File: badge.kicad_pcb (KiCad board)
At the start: 2 copper layers, 90 x 55 mm, 171 parts, among them P1 CONN_8, P2 CONN_11

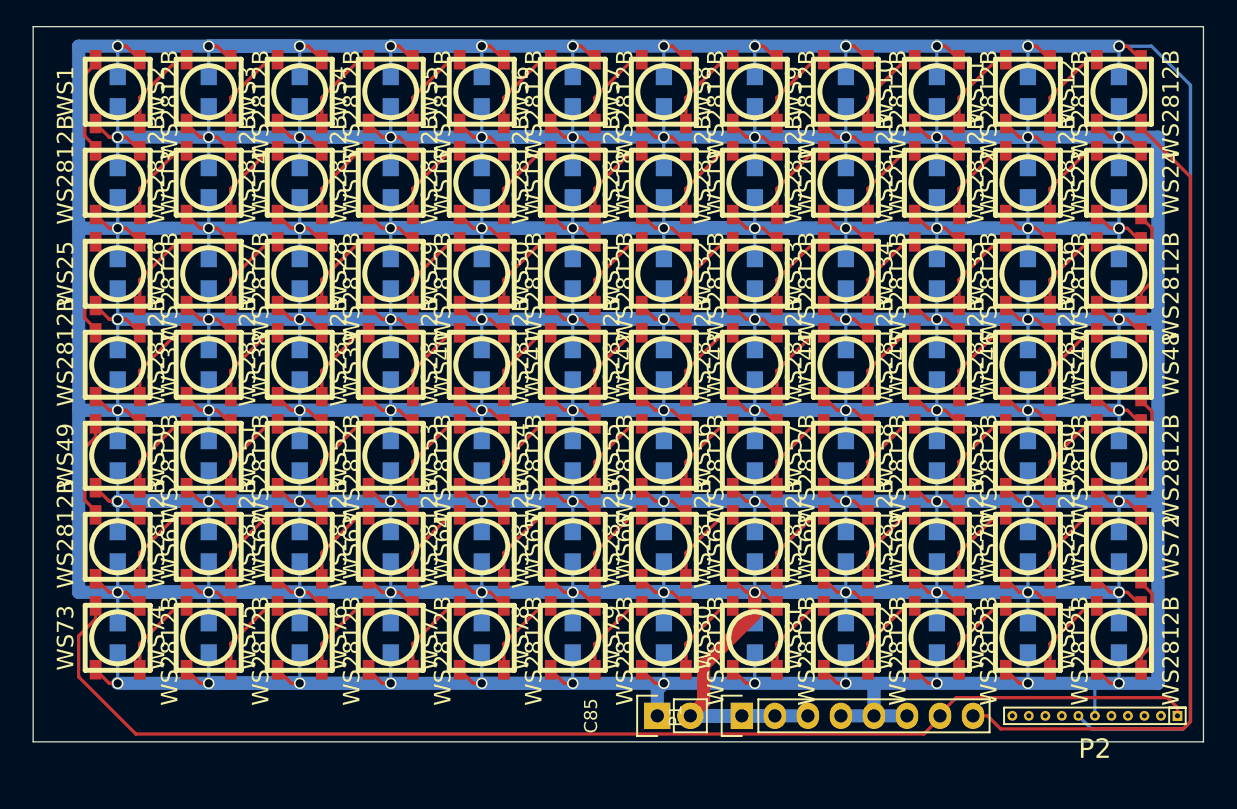
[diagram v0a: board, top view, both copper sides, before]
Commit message: Addition of second data input so we can unpopulate first and last row.
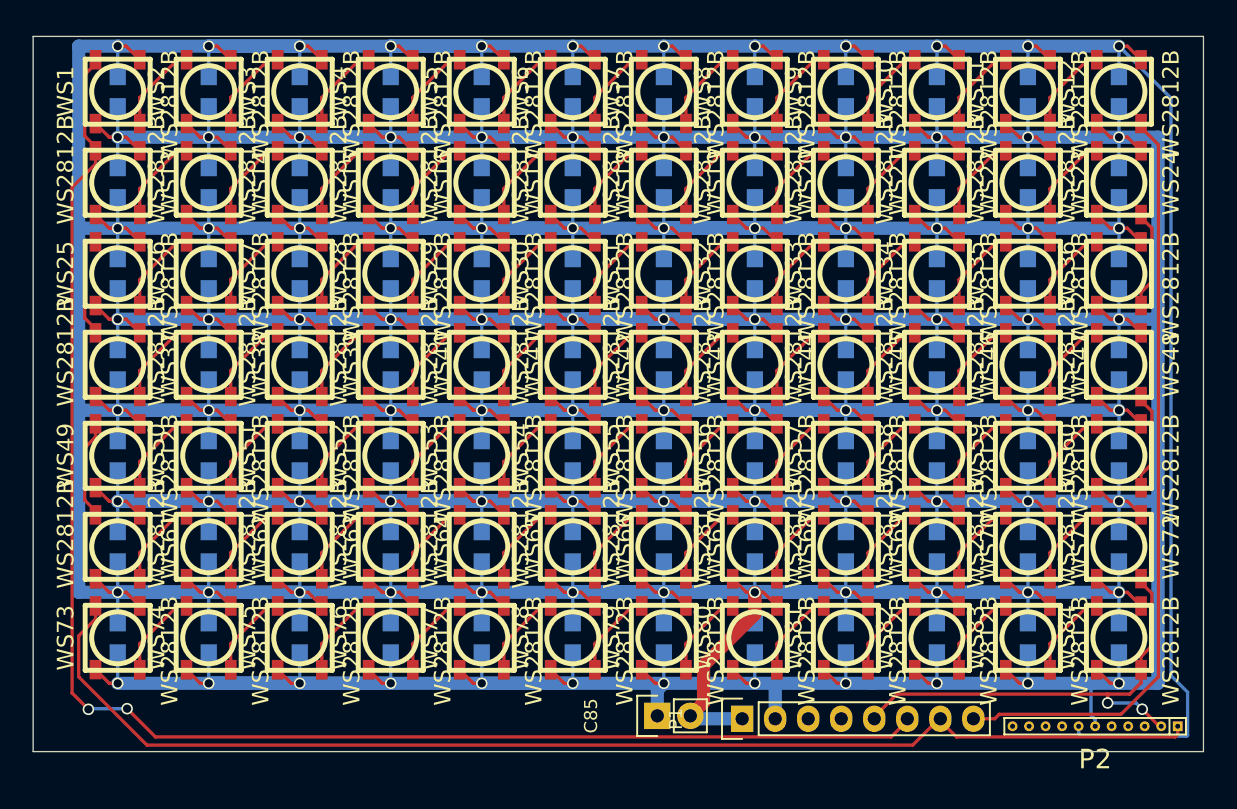
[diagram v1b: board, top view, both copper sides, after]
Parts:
- moved P2 0.80 mm to (103.0, 68.8)
- moved P1 0.23 mm to (69.5, 68.2)
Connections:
- P1 pad 2: /GND -> /VCC
- P1 pad 3: /GND -> (no net)
- P1 pad 4: /VCC -> (no net)
- P1 pad 5: /VCC -> /DIN2
- P1 pad 6: /VCC -> /DOUT2
- P2 pad 2: (no net) -> /DIN2
- WS1 pad 4: Net-(WS1-Pad4) -> /DOUT2
- WS13 pad 2: Net-(WS1-Pad4) -> /DOUT2
- WS72 pad 4: Net-(WS72-Pad4) -> /DIN2
- WS84 pad 2: Net-(WS72-Pad4) -> /DIN2
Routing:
- net /DOUT2: track 0.00 -> 116.6 mm, vias 0 -> 2
- net /DIN2: track 0.00 -> 36.6 mm, vias 0 -> 2
- net /GND: track 1225.3 -> 1209.2 mm
- net Net-(WS72-Pad4): track 7.69 -> 0.00 mm
- net Net-(WS1-Pad4): track 7.69 -> 0.00 mm
- net /DOUT: track 64.9 -> 58.7 mm
- net /VCC: track 981.3 -> 977.6 mm
- net /DIN: track 94.6 -> 95.8 mm

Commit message: Rev1 Added ground plan and mounting holes. Put some labels on silkscreen.
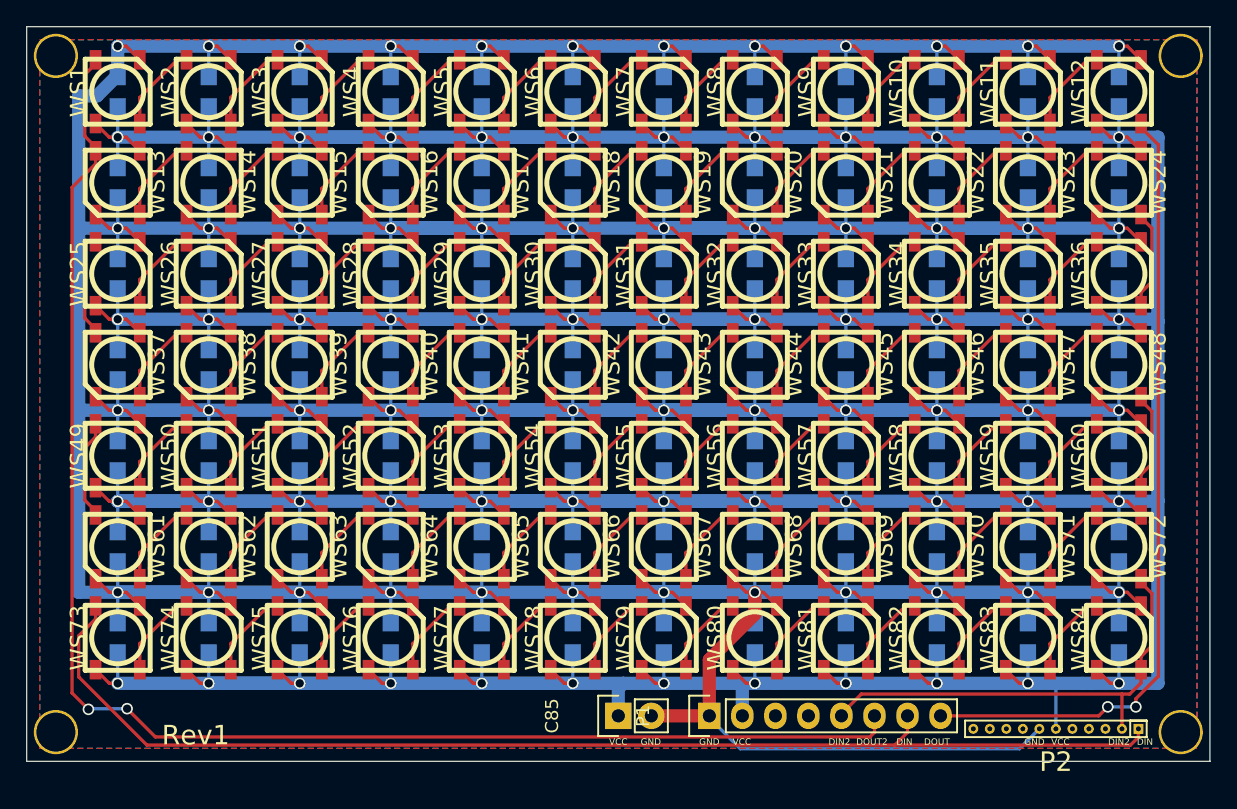
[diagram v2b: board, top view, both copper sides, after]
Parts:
- added REF**: 1PIN, badge:1PIN, F.Cu at (16.8, 17.2)
- added REF**: 1PIN, badge:1PIN, F.Cu at (103.2, 17.2)
- added REF**: 1PIN, badge:1PIN, F.Cu at (16.8, 69.2)
- added REF**: 1PIN, badge:1PIN, F.Cu at (103.2, 69.2)
- moved P2 3.03 mm to (100.0, 69.0)
- moved C85 3.00 mm to (60.0, 68.0)
- moved P1 2.54 mm to (67.0, 68.0)
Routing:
- net /GND: track 1209.2 -> 1170.9 mm
- net /DOUT: track 58.7 -> 61.4 mm, vias 0 -> 2
- net /DIN: track 95.8 -> 93.2 mm
- net /DOUT2: track 116.6 -> 114.7 mm
- net /DIN2: track 36.6 -> 35.6 mm, vias 2 -> 0
- added copper zone on B.Cu, net /GND
- added copper zone on F.Cu, net /GND
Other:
- board size 90 x 55 mm -> 91 x 56.5 mm
- board text added: "DIN"
- board text added: "DIN2"
- board text added: "DOUT"
- board text added: "DOUT2"
- board text added: "GND"
- board text added: "Rev1"
- board text added: "VCC"
